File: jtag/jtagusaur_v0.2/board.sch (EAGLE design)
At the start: 42 parts, among them J1 AVR_SPI_PRG_62X3_LOCK, U1 ATMEGA328P, Y1 16MHz

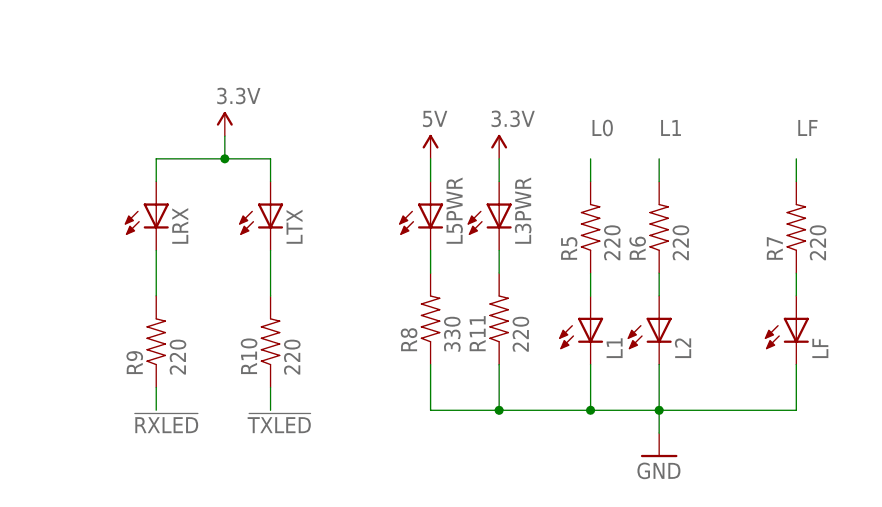
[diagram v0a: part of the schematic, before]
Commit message: update some of these values for the leds I decided to populate and their respective brightnesses
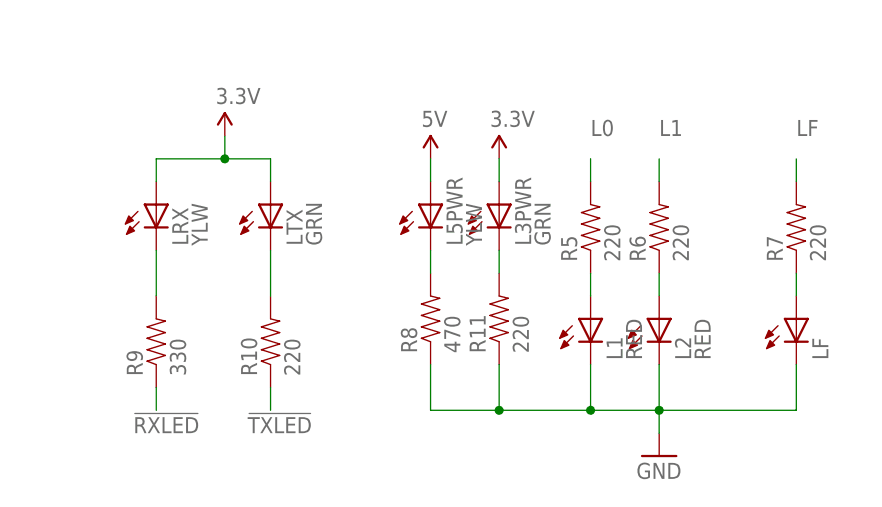
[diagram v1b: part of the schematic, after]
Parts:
- L1, L2: value (none) -> RED
- L3PWR, LTX: value (none) -> GRN
- L5PWR, LRX: value (none) -> YLW
- R8: value 330 -> 470
- R9: value 220 -> 330
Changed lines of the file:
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@@
 <?xml version="1.0" encoding="utf-8"?>
 <!DOCTYPE eagle SYSTEM "eagle.dtd">
-<eagle version="6.4">
+<eagle version="6.5.0">
 <drawing>
 <settings>
@@
 <part name="GND13" library="kmod-nonparts" deviceset="GND" device=""/>
 <part name="Y1" library="SparkFun-FreqCtrl" deviceset="CRYSTAL" device="HC49US" value="16MHz"/>
-<part name="L1" library="kmod-passives" deviceset="LED" device="0603"/>
-<part name="L2" library="kmod-passives" deviceset="LED" device="0603"/>
+<part name="L1" library="kmod-passives" deviceset="LED" device="0603" value="RED"/>
+<part name="L2" library="kmod-passives" deviceset="LED" device="0603" value="RED"/>
 <part name="LF" library="kmod-passives" deviceset="LED" device="0603"/>
 <part name="R5" library="kmod-passives" deviceset="RESISTOR" device="0603" value="220"/>
@@
 <part name="GND10" library="kmod-nonparts" deviceset="GND" device=""/>
 <part name="U$5" library="kmod-testing" deviceset="TXB0104" device="PWR"/>
-<part name="L5PWR" library="kmod-passives" deviceset="LED" device="0603"/>
-<part name="R8" library="kmod-passives" deviceset="RESISTOR" device="0603" value="330"/>
-<part name="R9" library="kmod-passives" deviceset="RESISTOR" device="0603" value="220"/>
+<part name="L5PWR" library="kmod-passives" deviceset="LED" device="0603" value="YLW"/>
+<part name="R8" library="kmod-passives" deviceset="RESISTOR" device="0603" value="470"/>
+<part name="R9" library="kmod-passives" deviceset="RESISTOR" device="0603" value="330"/>
 <part name="R10" library="kmod-passives" deviceset="RESISTOR" device="0603" value="220"/>
-<part name="LRX" library="kmod-passives" deviceset="LED" device="0603"/>
-<part name="LTX" library="kmod-passives" deviceset="LED" device="0603"/>
+<part name="LRX" library="kmod-passives" deviceset="LED" device="0603" value="YLW"/>
+<part name="LTX" library="kmod-passives" deviceset="LED" device="0603" value="GRN"/>
 <part name="C12" library="kmod-passives" deviceset="CAP" device="0402-CAP" value="22pF"/>
 <part name="C13" library="kmod-passives" deviceset="CAP" device="0402-CAP" value="22pF"/>
@@
 <part name="J1" library="SparkFun-Connectors" deviceset="AVR_SPI_PRG_6" device="2X3_LOCK"/>
 <part name="RA1" library="kmod-passives" deviceset="RESISTOR_ARRAY" device="0603_X4" value="100R"/>
-<part name="L3PWR" library="kmod-passives" deviceset="LED" device="0603"/>
+<part name="L3PWR" library="kmod-passives" deviceset="LED" device="0603" value="GRN"/>
 <part name="R11" library="kmod-passives" deviceset="RESISTOR" device="0603" value="220"/>
 <part name="SUPPLY7" library="kmod-nonparts" deviceset="5V" device=""/>
